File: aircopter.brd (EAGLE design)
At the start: 47 x 28 mm, 44 parts, among them IC1 STF202-22T1G, M1 WIRELESS-NRF24L01, U2 GY-521MPU6050, Y1 20 MHz

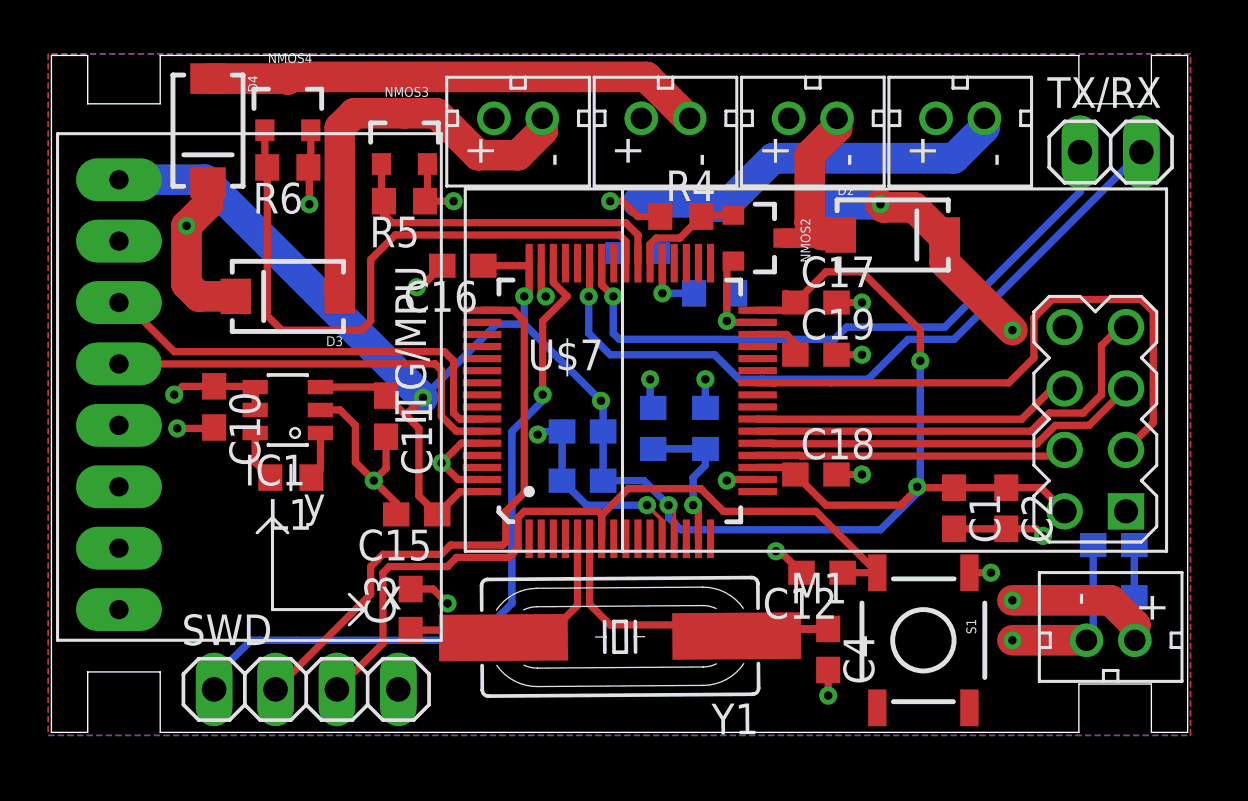
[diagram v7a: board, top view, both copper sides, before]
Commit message: "Added vias to help with bottlenecking and resized the 3v7 plane"
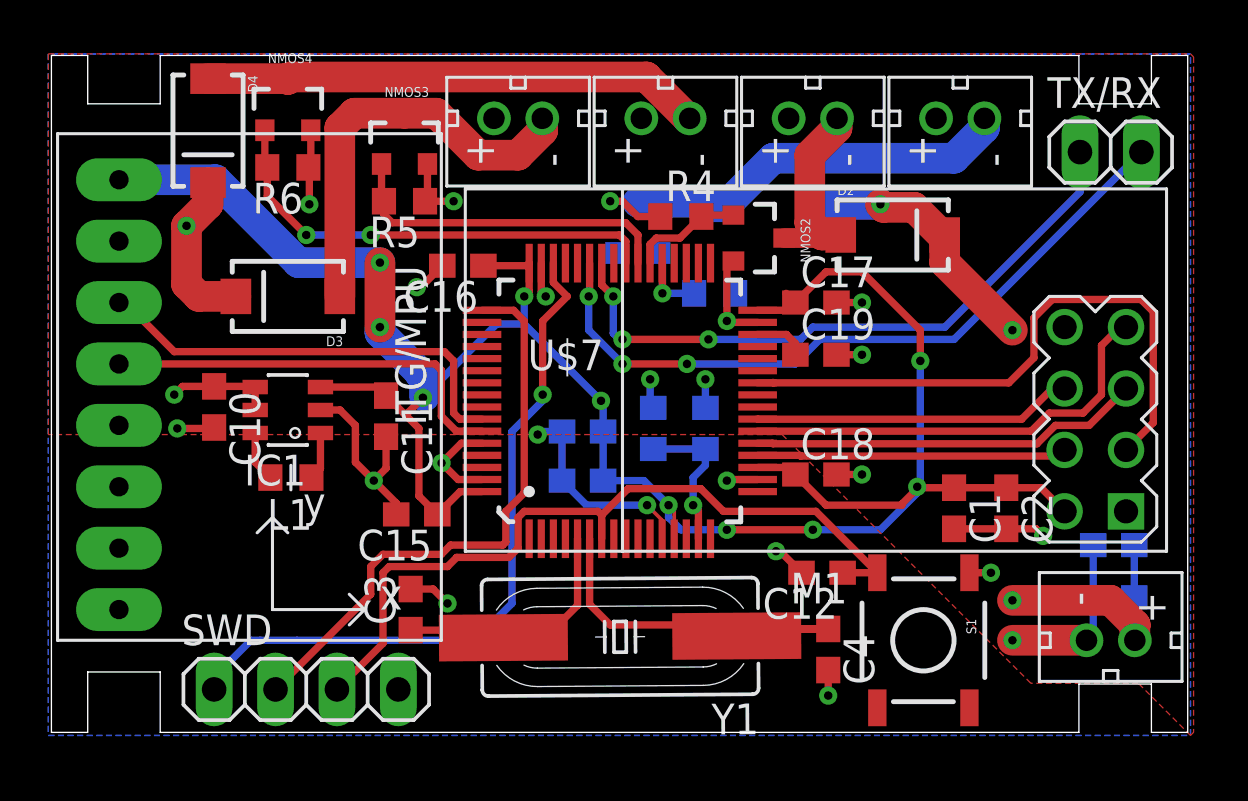
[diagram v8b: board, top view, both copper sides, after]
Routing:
- net PWM4: track 26.9 -> 19.3 mm, vias 0 -> 2
- net 3V3: track 92.4 -> 94.6 mm, vias 6 -> 10
- net RX: track 30.7 -> 30.1 mm, vias 1 -> 3
- net TX: vias 1 -> 3
